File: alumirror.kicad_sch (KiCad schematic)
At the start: 77 parts, among them J1 USB_C_Receptacle_USB2.0_16P_2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, J2 USB_C_Receptacle_USB2.0_16P_2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, K00 PG1350, K01 PG1350, K02 PG1350, K03 PG1350, K04 PG1350, K05 PG1350, K10 PG1350, K11 PG1350, K12 PG1350, K13 PG1350, K14 PG1350, K15 PG1350, K20 PG1350, K21 PG1350, K22 PG1350, K23 PG1350, K24 PG1350, K25 PG1350_1½U, K30 PG1350_1½U, K31 PG1350/SKQUCAA010, SW1 BOOT, U1 CH552T, U2 CH552T, U3 USBLC6-2P6, U4 USBLC6-2P6

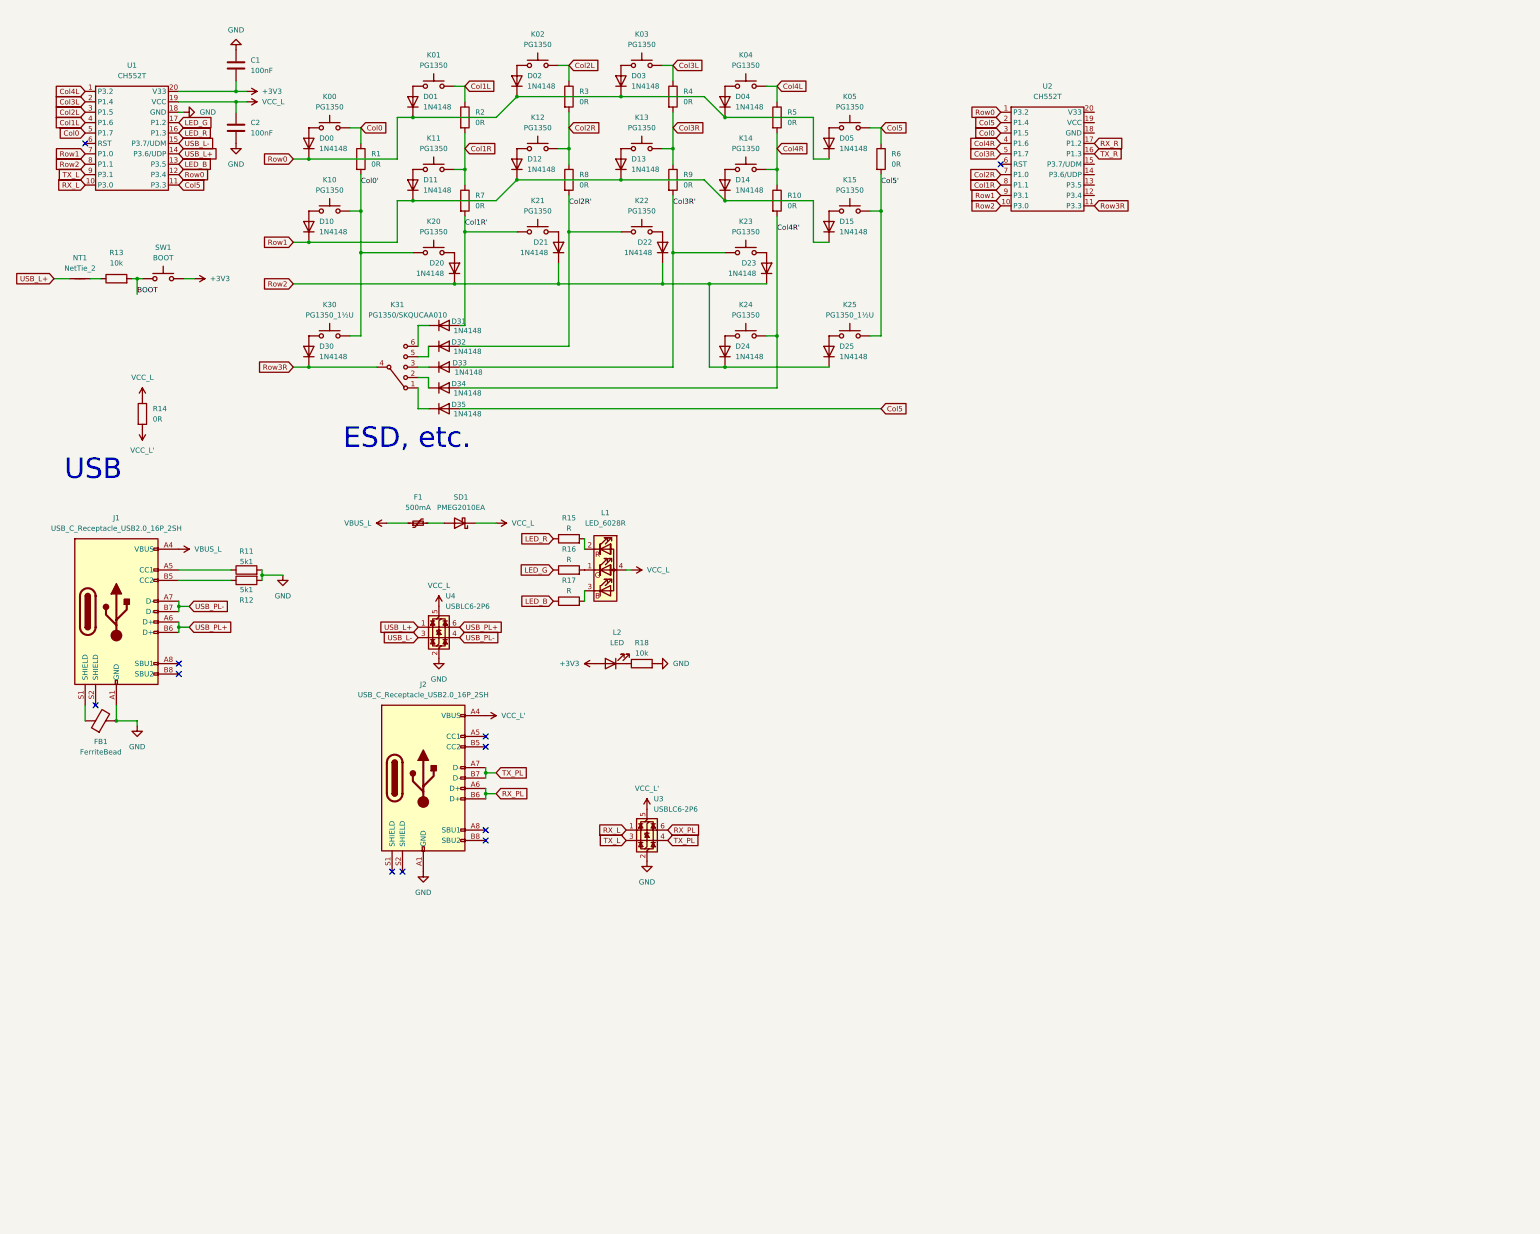
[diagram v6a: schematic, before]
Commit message: Add righthand active components
Routing is **very** rough
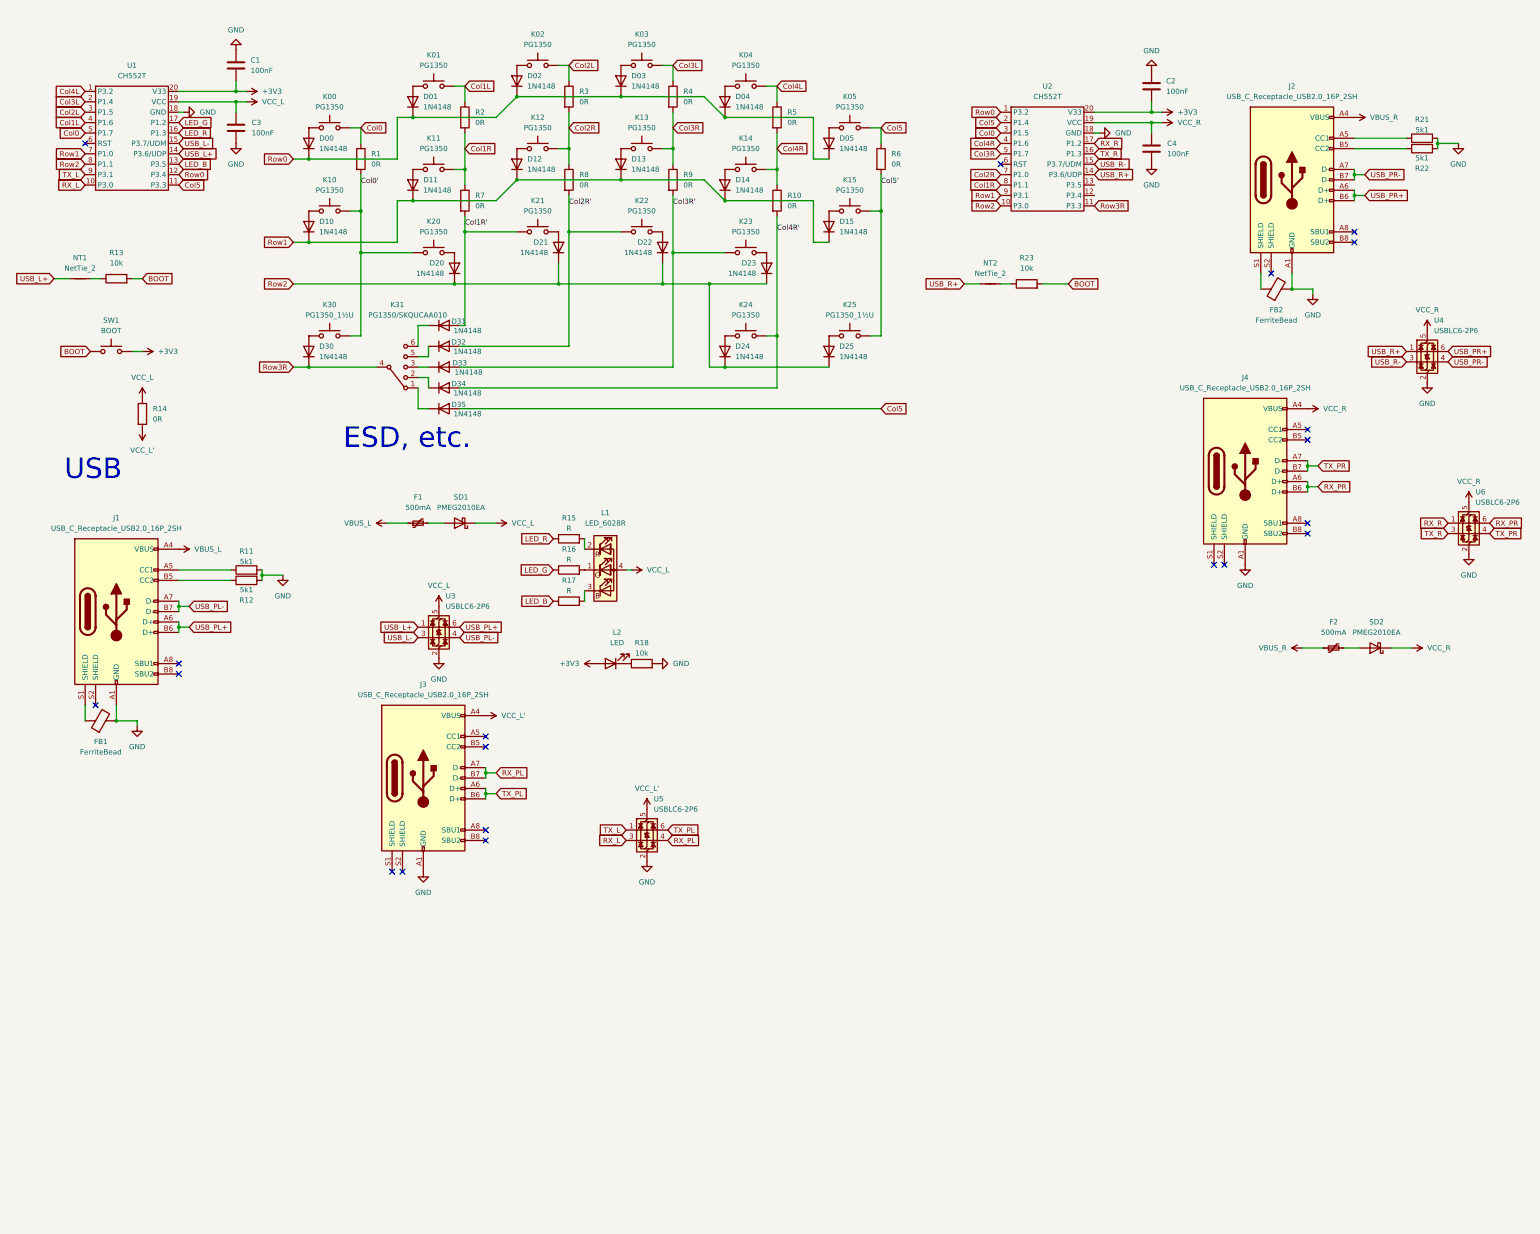
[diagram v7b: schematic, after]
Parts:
- added C2, C4: 100nF, Capacitor_SMD:C_0603_1608Metric, symbol Device:C
- added F2: 500mA, Fuse:Fuse_0603_1608Metric, symbol Device:Polyfuse_Small
- added FB2: FerriteBead, Inductor_SMD:L_0805_2012Metric, symbol Device:FerriteBead
- added J2, J4: USB_C_Receptacle_USB2.0_16P_2SH, Project Library:USB_C_Receptacle_HRO_TYPE-C-31-M-12, symbol Project Library:USB_C_Receptacle_USB2.0_16P_2SH
- added NT2: NetTie_2, Project Library:NetTie-2_SMD_Pad0.2mm, symbol Device:NetTie_2
- added R21, R22: 5k1, Project Library:R_0603_1608Metric_Mod, symbol Device:R
- added R23: 10k, Project Library:R_0603_1608Metric_Mod, symbol Device:R
- added SD2: PMEG2010EA, Diode_SMD:D_SOD-323, symbol Device:D_Schottky
- added U4, U6: USBLC6-2P6, Package_TO_SOT_SMD:SOT-666, symbol Power_Protection:USBLC6-2P6
- renumbered C2 to C3, J2 to J3, U4 to U3, U3 to U5
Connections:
- net +3V3: now also U2.20 (V33), C2.1
- net BOOT: now also R23.2
- net GND: now also U2.18 (GND), C2.2, C4.2, FB2.2, J2.A1 (GND), J2.A12 (GND), J2.B1 (GND), J2.B12 (GND), J4.A1 (GND), J4.A12 (GND), J4.B1 (GND), J4.B12 (GND), R21.2, R22.2, U4.2 (GND), U6.2 (GND)
- net RX_L: now also U5.3 (I/O2); no longer U5.1 (I/O1)
- net RX_PL: now also J3.A7 (D-), J3.B7 (D-), U5.4 (I/O2); no longer J3.A6 (D+), J3.B6 (D+), U5.6 (I/O1)
- net RX_R: now also U6.1 (I/O1)
- net TX_L: now also U5.1 (I/O1); no longer U5.3 (I/O2)
- net TX_PL: now also J3.A6 (D+), J3.B6 (D+), U5.6 (I/O1); no longer J3.A7 (D-), J3.B7 (D-), U5.4 (I/O2)
- net TX_R: now also U6.3 (I/O2)
- net USB_R+: now reaches U2.14 (P3.6/UDP)
- net USB_R+: now also NT2.1, U4.1 (I/O1)
- net USB_R-: now reaches U2.15 (P3.7/UDM)
- net USB_R-: now also U4.3 (I/O2)
- net VCC_R: now reaches U2.19 (VCC)
- net VCC_R: now also C4.1, J4.A4 (VBUS), J4.A9 (VBUS), J4.B4 (VBUS), J4.B9 (VBUS), SD2.1 (K), U4.5 (VBUS), U6.5 (VBUS)
- new net: J2.A5 (CC1), R21.1
- new net: J2.B5 (CC2), R22.1
- new net: FB2.1, J2.S1 (SHIELD)
- new net: F2.2, SD2.2 (A)
- new net: NT2.2, R23.1
- new net RX_PR: J4.A6 (D+), J4.B6 (D+), U6.6 (I/O1)
- new net TX_PR: J4.A7 (D-), J4.B7 (D-), U6.4 (I/O2)
- new net USB_PR+: J2.A6 (D+), J2.B6 (D+), U4.6 (I/O1)
- new net USB_PR-: J2.A7 (D-), J2.B7 (D-), U4.4 (I/O2)
- new net VBUS_R: F2.1, J2.A4 (VBUS), J2.A9 (VBUS), J2.B4 (VBUS), J2.B9 (VBUS)
- no-connect marks 11 -> 20

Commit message: Tidy schematic
Matrix is broken out into a separate sheet
Controller components are more organised
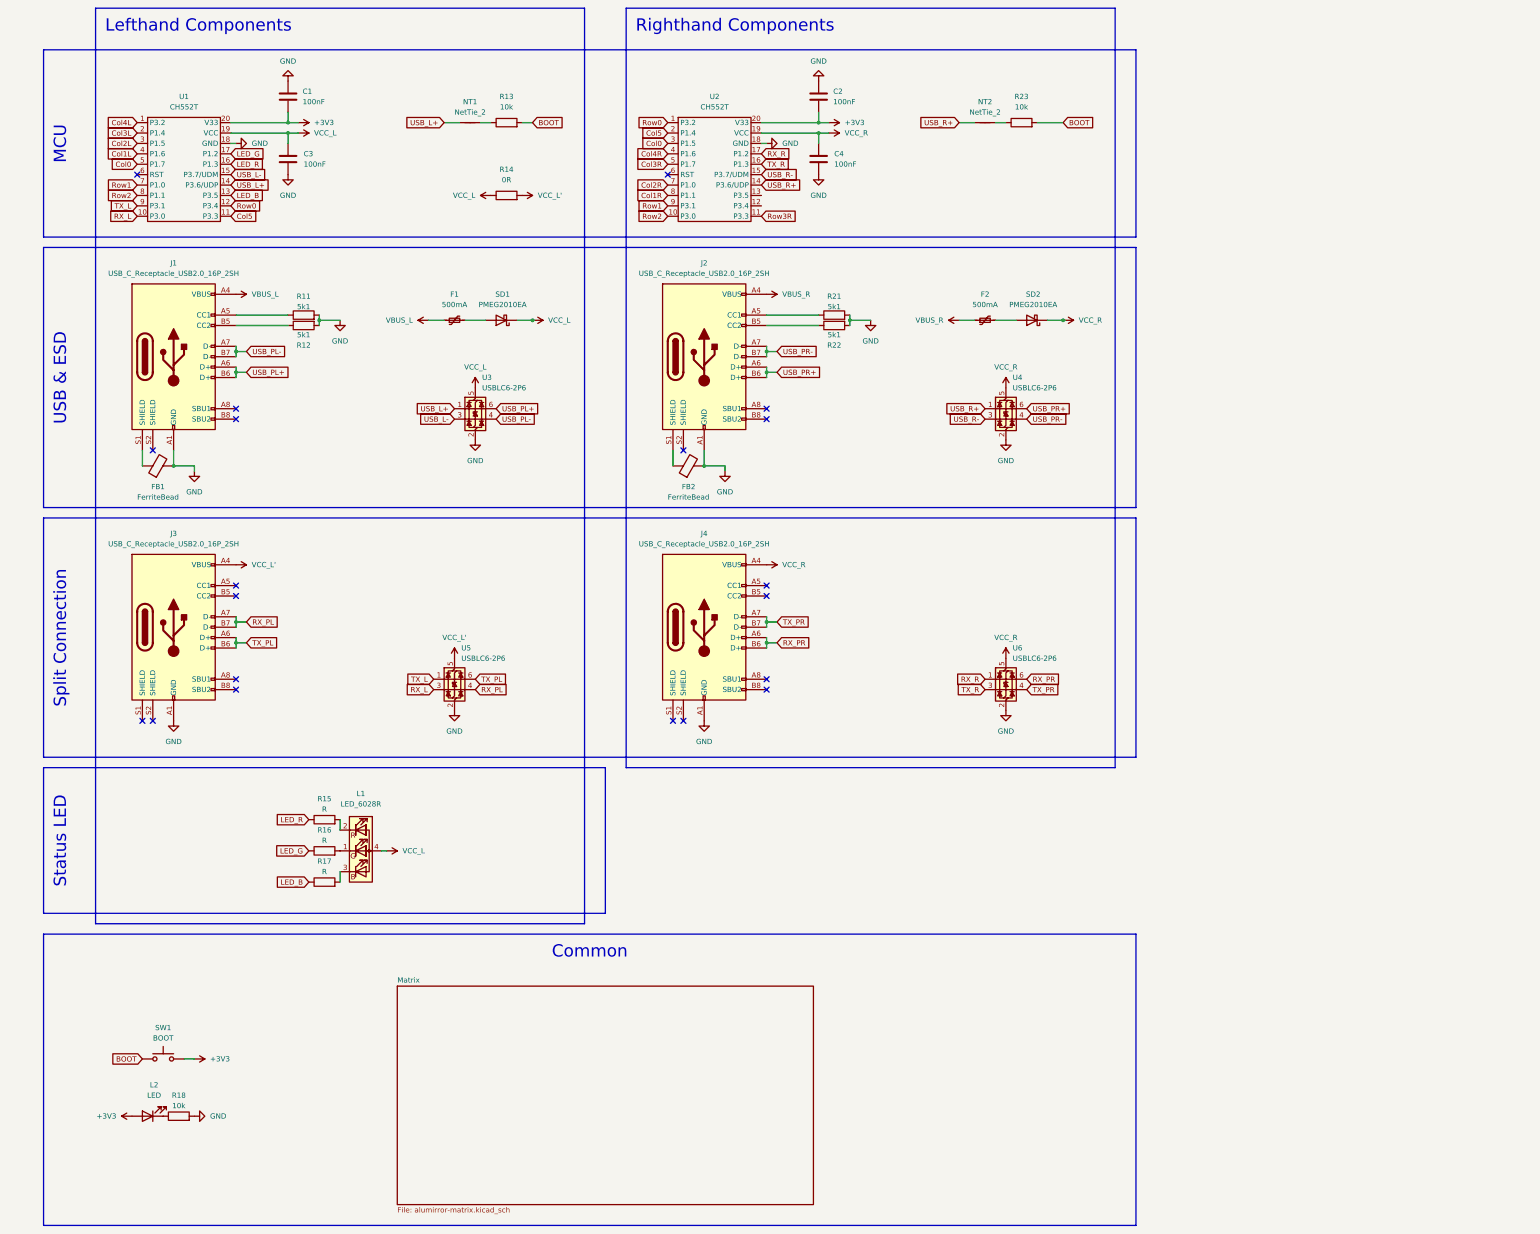
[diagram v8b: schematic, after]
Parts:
- removed D00, D01, D02, D03, D04, D05, D10, D11, D12, D13, D14, D15, D20, D21, D22, D23, D24, D25, D30, D31, D32, D33, D34, D35: 1N4148, Project Library:D_SOD-123_Mod, symbol Device:D
- removed K00, K01, K02, K03, K04, K05, K10, K11, K12, K13, K14, K15, K20, K21, K22, K23, K24: PG1350, Project Library:SW_choc_v1_HS_CPG135001S30_1layer_1u, symbol Switch:SW_Push
- removed K25, K30: PG1350_1½U, Project Library:SW_choc_v1_HS_CPG135001S30_1layer_1.5u, symbol Switch:SW_Push
- removed K31: PG1350/SKQUCAA010, Project Library:SW_choc_v1_HS_nav_CPG135001S30_SKQUCAA010_1layer_1u_1, symbol Project Library:SW_SP5T
- removed R1, R10, R2, R3, R4, R5, R6, R7, R8, R9: 0R, Project Library:R_2010_5025Metric_Mod, symbol Device:R
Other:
- added sheet Matrix (alumirror-matrix.kicad_sch)
- note removed: "ESD, etc."
- note removed: "USB"
- title: (none) -> Alumirror 
- moved on the sheet: C1, C2, C3, C4, F1, FB1, FB2, J1, J2, J3, J4, L1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
